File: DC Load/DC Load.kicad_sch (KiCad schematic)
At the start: 53 parts, among them IC1 OPA277UA, IC2 LTC1046CS8#PBF, IC3 DAC80501MDGST, J1 VSENSE, J2 LOAD_POS, J3 LOAD_NEG, J4 DC 15V..18V, U10 MC7805BD2TR4G, U7 MCP3426, U8 OPA2182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

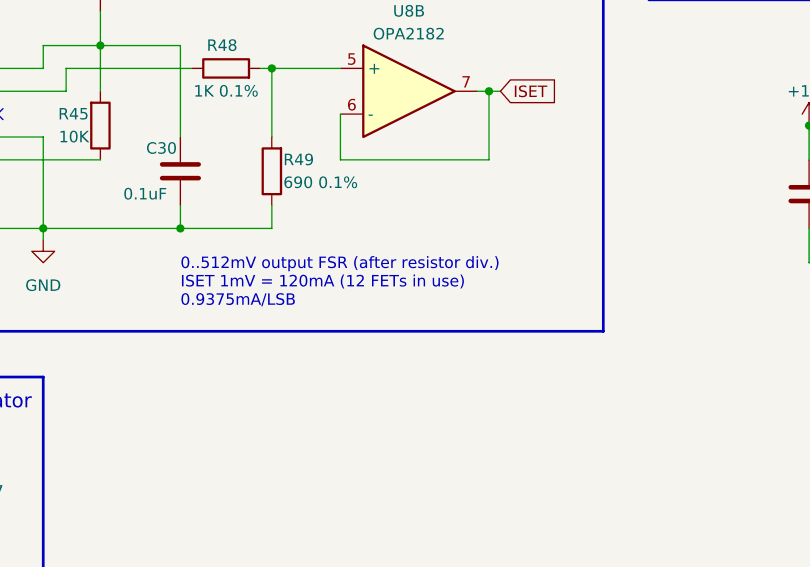
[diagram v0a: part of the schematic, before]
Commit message: Use 8 load FETS instead of 12
Using 8 FETS makes output resolution easier to calculate when using a power of two volatage reference in the output DAC. Also cheaper and it's easier to fit fewer devices onto the heatsink area.
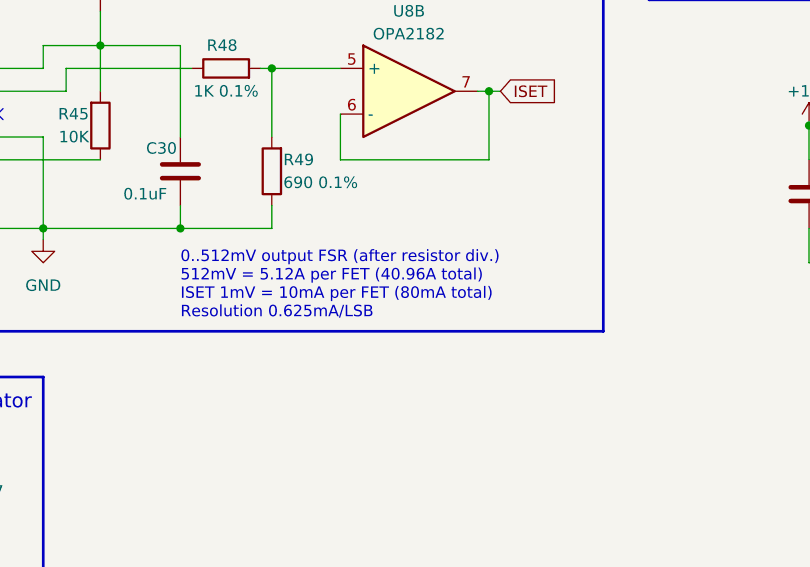
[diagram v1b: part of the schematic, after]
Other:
- note added: "0..512mV output FSR (after resistor div.) 512mV = 5.12A per FET (40.96A total) ISET 1mV = 10mA per FET (80mA total) Resolution 0.625mA/LSB"
- note removed: "0..512mV output FSR (after resistor div.) ISET 1mV = 120mA (12 FETs in use) 0.9375mA/LSB"
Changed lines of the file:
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@@
     (effects (font (size 1.27 1.27)) (justify left bottom))
   )
-  (text "0..512mV output FSR (after resistor div.)\nISET 1mV = 120mA (12 FETs in use)\n0.9375mA/LSB"
-    (at 177.8 147.32 0)
+  (text "0..512mV output FSR (after resistor div.)\n512mV = 5.12A per FET (40.96A total)\nISET 1mV = 10mA per FET (80mA total)\nResolution 0.625mA/LSB"
+    (at 177.8 148.59 0)
     (effects (font (size 1.27 1.27)) (justify left bottom))
   )
@@
       (reference "#PWR07") (unit 1) (value "+12V") (footprint "")
     )
-    (path "/dbf2ec6d-5b7c-4864-8414-3433d3b742de/077f44d5-616d-430e-90f9-fddf0da69b64"
-      (reference "#PWR08") (unit 1) (value "+12V") (footprint "")
-    )
-    (path "/dbf2ec6d-5b7c-4864-8414-3433d3b742de/8ef0858f-8f99-4074-8e5d-12a5cac189a5"
-      (reference "#PWR09") (unit 1) (value "+12V") (footprint "")
-    )
     (path "/dbf2ec6d-5b7c-4864-8414-3433d3b742de/3fec2d76-ae4a-4c52-a705-9aa4fc1d6e0a"
       (reference "#PWR010") (unit 1) (value "GND") (footprint "")
     )
-    (path "/dbf2ec6d-5b7c-4864-8414-3433d3b742de/b3782ebd-b233-497b-bca1-dc0becb54394"
-      (reference "#PWR011") (unit 1) (value "GND") (footprint "")
-    )
-    (path "/dbf2ec6d-5b7c-4864-8414-3433d3b742de/e580df66-2099-4ccc-ab19-3e9c5ac519dd"
-      (reference "#PWR012") (unit 1) (value "GND") (footprint "")
-    )
     (path "/c4c59f0d-79cb-4ca8-8ea9-a58a005d680b"
       (reference "#PWR013") (unit 1) (value "+5V") (footprint "")
@@
       (reference "C8") (unit 1) (value "0.1uF") (footprint "")
     )
-    (path "/dbf2ec6d-5b7c-4864-8414-3433d3b742de/48e54bae-99d4-47fd-8725-e356ed12a559"
-      (reference "C9") (unit 1) (value "1uF") (footprint "")
-    )
-    (path "/dbf2ec6d-5b7c-4864-8414-3433d3b742de/8ae8686e-c16f-4da9-83b5-9352b825780a"
-      (reference "C10") (unit 1) (value "0.1uF") (footprint "")
-    )
-    (path "/dbf2ec6d-5b7c-4864-8414-3433d3b742de/d9098321-3649-4d94-8c55-daa5b8640f7e"
-      (reference "C11") (unit 1) (value "1uF") (footprint "")
-    )
-    (path "/dbf2ec6d-5b7c-4864-8414-3433d3b742de/4ee37b27-6692-410d-9045-cd3fe66be3c3"
-      (reference "C12") (unit 1) (value "0.1uF") (footprint "")
-    )
     (path "/0e459836-9f92-4e69-890e-9a3ede46b74f"
       (reference "C13") (unit 1) (value "0.1uF") (footprint "")
@@
       (reference "Q8") (unit 1) (value "IRFP260") (footprint "Package_TO_SOT_THT:TO-247-3_Vertical")
     )
-    (path "/dbf2ec6d-5b7c-4864-8414-3433d3b742de/93d1bd71-652f-471c-8184-c4174650db6b"
-      (reference "Q9") (unit 1) (value "IRFP260") (footprint "Package_TO_SOT_THT:TO-247-3_Vertical")
-    )
-    (path "/dbf2ec6d-5b7c-4864-8414-3433d3b742de/05078bbe-64aa-4f37-a9be-be09d2b91aad"
-      (reference "Q10") (unit 1) (value "IRFP260") (footprint "Package_TO_SOT_THT:TO-247-3_Vertical")
-    )
-    (path "/dbf2ec6d-5b7c-4864-8414-3433d3b742de/24fd4026-e1d2-4d16-8371-a7ae504cea54"
-      (reference "Q11") (unit 1) (value "IRFP260") (footprint "Package_TO_SOT_THT:TO-247-3_Vertical")
-    )
-    (path "/dbf2ec6d-5b7c-4864-8414-3433d3b742de/f716d792-3701-4212-8bd7-b2aa50d9d16d"
-      (reference "Q12") (unit 1) (value "IRFP260") (footprint "Package_TO_SOT_THT:TO-247-3_Vertical")
-    )
     (path "/dbf2ec6d-5b7c-4864-8414-3433d3b742de/bbe6c202-16d1-4580-8239-17871b71c2d9"
       (reference "R1") (unit 1) (value "10K") (footprint "")
@@
       (reference "R24") (unit 1) (value "0R1 1% 2W") (footprint "")
     )
-    (path "/dbf2ec6d-5b7c-4864-8414-3433d3b742de/88063cca-ca15-403d-9e05-db1ccdfe76a1"
-      (reference "R25") (unit 1) (value "10K") (footprint "")
-    )
-    (path "/dbf2ec6d-5b7c-4864-8414-3433d3b742de/c5b232d7-0c92-4bfd-a241-7bab335f5745"
-      (reference "R26") (unit 1) (value "10K") (footprint "")
-    )
-    (path "/dbf2ec6d-5b7c-4864-8414-3433d3b742de/5970c4ce-1d25-49ab-922e-e5634eadaeae"
-      (reference "R27") (unit 1) (value "10K") (footprint "")
-    )
-    (path "/dbf2ec6d-5b7c-4864-8414-3433d3b742de/b1150dc0-284c-49f8-890f-93432f37dc65"
-      (reference "R28") (unit 1) (value "10K") (footprint "")
-    )
-    (path "/dbf2ec6d-5b7c-4864-8414-3433d3b742de/8ed44255-5d02-4f31-b9bc-2fe46f120e9d"
-      (reference "R29") (unit 1) (value "200") (footprint "")
-    )
-    (path "/dbf2ec6d-5b7c-4864-8414-3433d3b742de/49d25e1e-0ffe-422c-b8bf-47171d26c524"
-      (reference "R30") (unit 1) (value "200") (footprint "")
-    )
-    (path "/dbf2ec6d-5b7c-4864-8414-3433d3b742de/1bf41b7a-7472-45f1-b60a-412a432f6768"
-      (reference "R31") (unit 1) (value "200") (footprint "")
-    )
-    (path "/dbf2ec6d-5b7c-4864-8414-3433d3b742de/5de34c36-34f4-4e78-b96b-630c36245947"
-      (reference "R32") (unit 1) (value "200") (footprint "")
-    )
-    (path "/dbf2ec6d-5b7c-4864-8414-3433d3b742de/d1d50d42-88e4-417e-9804-29ddd0511384"
-      (reference "R33") (unit 1) (value "0R1 1% 2W") (footprint "")
-    )
-    (path "/dbf2ec6d-5b7c-4864-8414-3433d3b742de/bf162598-cec0-4790-8ed6-22adf86c7fc2"
-      (reference "R34") (unit 1) (value "0R1 1% 2W") (footprint "")
-    )
-    (path "/dbf2ec6d-5b7c-4864-8414-3433d3b742de/796a7a72-46be-4d24-9d94-110726e2120a"
-      (reference "R35") (unit 1) (value "0R1 1% 2W") (footprint "")
-    )
-    (path "/dbf2ec6d-5b7c-4864-8414-3433d3b742de/b0663545-8ddb-473f-a22f-fbc1d78f09fe"
-      (reference "R36") (unit 1) (value "0R1 1% 2W") (footprint "")
-    )
     (path "/4411b0ef-e69b-42cb-9020-3bdf6c26c20a"
       (reference "R37") (unit 1) (value "1M") (footprint "")
@@
       (reference "U4") (unit 3) (value "OPA2182") (footprint "")
     )
-    (path "/dbf2ec6d-5b7c-4864-8414-3433d3b742de/94c61c18-d393-4ed2-b9a8-7b051066bd95"
-      (reference "U5") (unit 1) (value "OPA2182") (footprint "")
-    )
-    (path "/dbf2ec6d-5b7c-4864-8414-3433d3b742de/74a67f61-fa06-4b9b-bd26-940786d660a8"
-      (reference "U5") (unit 2) (value "OPA2182") (footprint "")
-    )
-    (path "/dbf2ec6d-5b7c-4864-8414-3433d3b742de/948c7406-d50f-4323-9be9-7e109ad003d5"
-      (reference "U5") (unit 3) (value "OPA2182") (footprint "")
-    )
-    (path "/dbf2ec6d-5b7c-4864-8414-3433d3b742de/d3eff3ff-0c8f-4683-b716-cf227e2df64c"
-      (reference "U6") (unit 1) (value "OPA2182") (footprint "")
-    )
-    (path "/dbf2ec6d-5b7c-4864-8414-3433d3b742de/7555a97a-a9b0-4ce3-bc6f-d58314f4edb3"
-      (reference "U6") (unit 2) (value "OPA2182") (footprint "")
-    )
-    (path "/dbf2ec6d-5b7c-4864-8414-3433d3b742de/ece7da38-3971-465d-a206-75edc31318e1"
-      (reference "U6") (unit 3) (value "OPA2182") (footprint "")
-    )
     (path "/65e23b4e-60b7-4086-8542-99cea00c4381"

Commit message: Bugfix - resistor in wrong spot
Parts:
- removed R47: 10K, symbol Device:R
- added R?: 10K, symbol Device:R
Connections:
- net GND: now also C29.1, R?.2
- net at IC3.7 (~{SYNC}/A0): now also R?.1; no longer C29.1
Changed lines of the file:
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@@
   (junction (at 82.55 151.13) (diameter 0) (color 0 0 0 0)
   )
+  (junction (at 111.76 138.43) (diameter 0) (color 0 0 0 0)
+  )
   (junction (at 72.39 170.18) (diameter 0) (color 0 0 0 0)
   )
@@
   )
   (junction (at 62.23 151.13) (diameter 0) (color 0 0 0 0)
-  )
-  (junction (at 119.38 138.43) (diameter 0) (color 0 0 0 0)
   )
   (junction (at 170.18 87.63) (diameter 0) (color 0 0 0 0)
@@
     (stroke (width 0) (type default) (color 0 0 0 0))
   )
+  (wire (pts (xy 109.22 120.65) (xy 111.76 120.65))
+    (stroke (width 0) (type default) (color 0 0 0 0))
+  )
   (wire (pts (xy 40.64 182.88) (xy 40.64 187.96))
     (stroke (width 0) (type default) (color 0 0 0 0))
@@
     (stroke (width 0.3) (type default) (color 0 0 0 0))
   )
-  (wire (pts (xy 111.76 120.65) (xy 111.76 138.43))
+  (wire (pts (xy 109.22 120.65) (xy 109.22 138.43))
     (stroke (width 0) (type default) (color 0 0 0 0))
   )
@@
     (stroke (width 0) (type default) (color 0 0 0 0))
   )
+  (wire (pts (xy 111.76 128.27) (xy 111.76 138.43))
+    (stroke (width 0) (type default) (color 0 0 0 0))
+  )
   (wire (pts (xy 31.75 151.13) (xy 40.64 151.13))
     (stroke (width 0) (type default) (color 0 0 0 0))
@@
     (stroke (width 0) (type default) (color 0 0 0 0))
   )
-  (wire (pts (xy 151.13 138.43) (xy 162.56 138.43))
-    (stroke (width 0) (type default) (color 0 0 0 0))
-  )
   (wire (pts (xy 87.63 151.13) (xy 82.55 151.13))
     (stroke (width 0) (type default) (color 0 0 0 0))
@@
     (stroke (width 0) (type default) (color 0 0 0 0))
   )
+  (wire (pts (xy 109.22 138.43) (xy 111.76 138.43))
+    (stroke (width 0) (type default) (color 0 0 0 0))
+  )
   (wire (pts (xy 72.39 49.53) (xy 78.74 49.53))
     (stroke (width 0) (type default) (color 0 0 0 0))
@@
     (stroke (width 0) (type default) (color 0 0 0 0))
   )
-  (wire (pts (xy 111.76 138.43) (xy 119.38 138.43))
-    (stroke (width 0) (type default) (color 0 0 0 0))
-  )
   (wire (pts (xy 185.42 34.29) (xy 185.42 44.45))
     (stroke (width 0) (type default) (color 0 0 0 0))
@@
     (stroke (width 0) (type default) (color 0 0 0 0))
   )
-  (wire (pts (xy 121.92 128.27) (xy 119.38 128.27))
-    (stroke (width 0) (type default) (color 0 0 0 0))
-  )
   (wire (pts (xy 198.12 33.02) (xy 198.12 38.1))
     (stroke (width 0) (type default) (color 0 0 0 0))
@@
     (stroke (width 0) (type default) (color 0 0 0 0))
   )
+  (wire (pts (xy 111.76 138.43) (xy 162.56 138.43))
+    (stroke (width 0) (type default) (color 0 0 0 0))
+  )
   (wire (pts (xy 130.81 49.53) (xy 139.7 49.53))
     (stroke (width 0) (type default) (color 0 0 0 0))
@@
     (stroke (width 0) (type default) (color 0 0 0 0))
   )
+  (wire (pts (xy 113.03 128.27) (xy 111.76 128.27))
+    (stroke (width 0) (type default) (color 0 0 0 0))
+  )
   (wire (pts (xy 40.64 151.13) (xy 40.64 146.05))
     (stroke (width 0) (type default) (color 0 0 0 0))
@@
     (stroke (width 0) (type default) (color 0 0 0 0))
   )
+  (wire (pts (xy 120.65 128.27) (xy 121.92 128.27))
+    (stroke (width 0) (type default) (color 0 0 0 0))
+  )
   (wire (pts (xy 204.47 58.42) (xy 204.47 68.58))
     (stroke (width 0) (type default) (color 0 0 0 0))
@@
     (stroke (width 0) (type default) (color 0 0 0 0))
   )
-  (wire (pts (xy 119.38 138.43) (xy 143.51 138.43))
-    (stroke (width 0) (type default) (color 0 0 0 0))
-  )
   (wire (pts (xy 189.23 90.17) (xy 191.77 90.17))
     (stroke (width 0) (type default) (color 0 0 0 0))
@@
   (polyline (pts (xy 92.71 195.58) (xy 92.71 116.84))
     (stroke (width 0.3) (type default) (color 0 0 0 0))
-  )
-  (wire (pts (xy 119.38 128.27) (xy 119.38 138.43))
-    (stroke (width 0) (type default) (color 0 0 0 0))
   )
   (text "Negative Voltage Generator\n" (at 161.29 158.75 180)
@@
     (effects (font (size 0.8 0.8)) (justify left bottom))
   )
-  (text "Internal Ref 1.25V\n19.07349uV/LSB" (at 123.19 144.78 0)
+  (text "Internal Ref 1.25V\n19.07349uV/LSB" (at 130.81 138.43 0)
     (effects (font (size 1.27 1.27)) (justify left bottom))
   )
@@
     (pin "3")
   )
-  (symbol (lib_id "Device:R") (at 147.32 138.43 270) (mirror x) (unit 1)
-    (in_bom yes) (on_board yes)
-    (property "Reference" "R47" (id 0) (at 148.59 135.89 90)
-      (effects (font (size 1.27 1.27)) (justify right))
-    )
-    (property "Value" "10K" (id 1) (at 147.32 138.43 90))
-    (property "Footprint" "" (id 2) (at 147.32 140.208 90)
-      (effects (font (size 1.27 1.27)) hide)
-    )
-    (property "Datasheet" "~" (id 3) (at 147.32 138.43 0)
-      (effects (font (size 1.27 1.27)) hide)
-    )
-    (pin "1")
-    (pin "2")
-  )
   (symbol (lib_id "Device:R") (at 139.7 57.15 180) (unit 1)
     (in_bom yes) (on_board yes)
@@
     )
     (pin "1")
+  )
+  (symbol (lib_id "Device:R") (at 116.84 128.27 270) (mirror x) (unit 1)
+    (in_bom yes) (on_board yes)
+    (property "Reference" "R?" (id 0) (at 114.3 127 90)
+      (effects (font (size 1.27 1.27)) (justify right))
+    )
+    (property "Value" "10K" (id 1) (at 116.84 128.27 90))
+    (property "Footprint" "" (id 2) (at 116.84 130.048 90)
+      (effects (font (size 1.27 1.27)) hide)
+    )
+    (property "Datasheet" "~" (id 3) (at 116.84 128.27 0)
+      (effects (font (size 1.27 1.27)) hide)
+    )
+    (pin "1")
+    (pin "2")
   )
   (symbol (lib_id "Regulator_Linear:L7812") (at 62.23 133.35 0) (unit 1)
@@
       (reference "R46") (unit 1) (value "100") (footprint "")
     )
-    (path "/935fb03b-f0db-42c1-a4f7-2430ad426b9e"
-      (reference "R47") (unit 1) (value "10K") (footprint "")
-    )
     (path "/7e64c2a3-8c3f-4afb-9429-7a603e43e43e"
       (reference "R48") (unit 1) (value "1K 0.1%") (footprint "")
@@
       (reference "R49") (unit 1) (value "690 0.1%") (footprint "")
     )
+    (path "/b9c5f949-0e6d-48da-b377-b5d78bd4b540"
+      (reference "R?") (unit 1) (value "10K") (footprint "")
+    )
     (path "/bd52a1b1-d864-4933-bd41-0b4f09530fa4"
